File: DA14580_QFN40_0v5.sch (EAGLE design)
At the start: 29 parts, among them CON1 CON_TC2030-CTL-NL, IC1 1265-1137-1-ND, IC2 74LVC1G00DBV, IC3 IC_LDO_XX1117_5, U1 DA14583-AT2, X1 SSW-114-02-S-S, X2 SSW-114-02-S-S

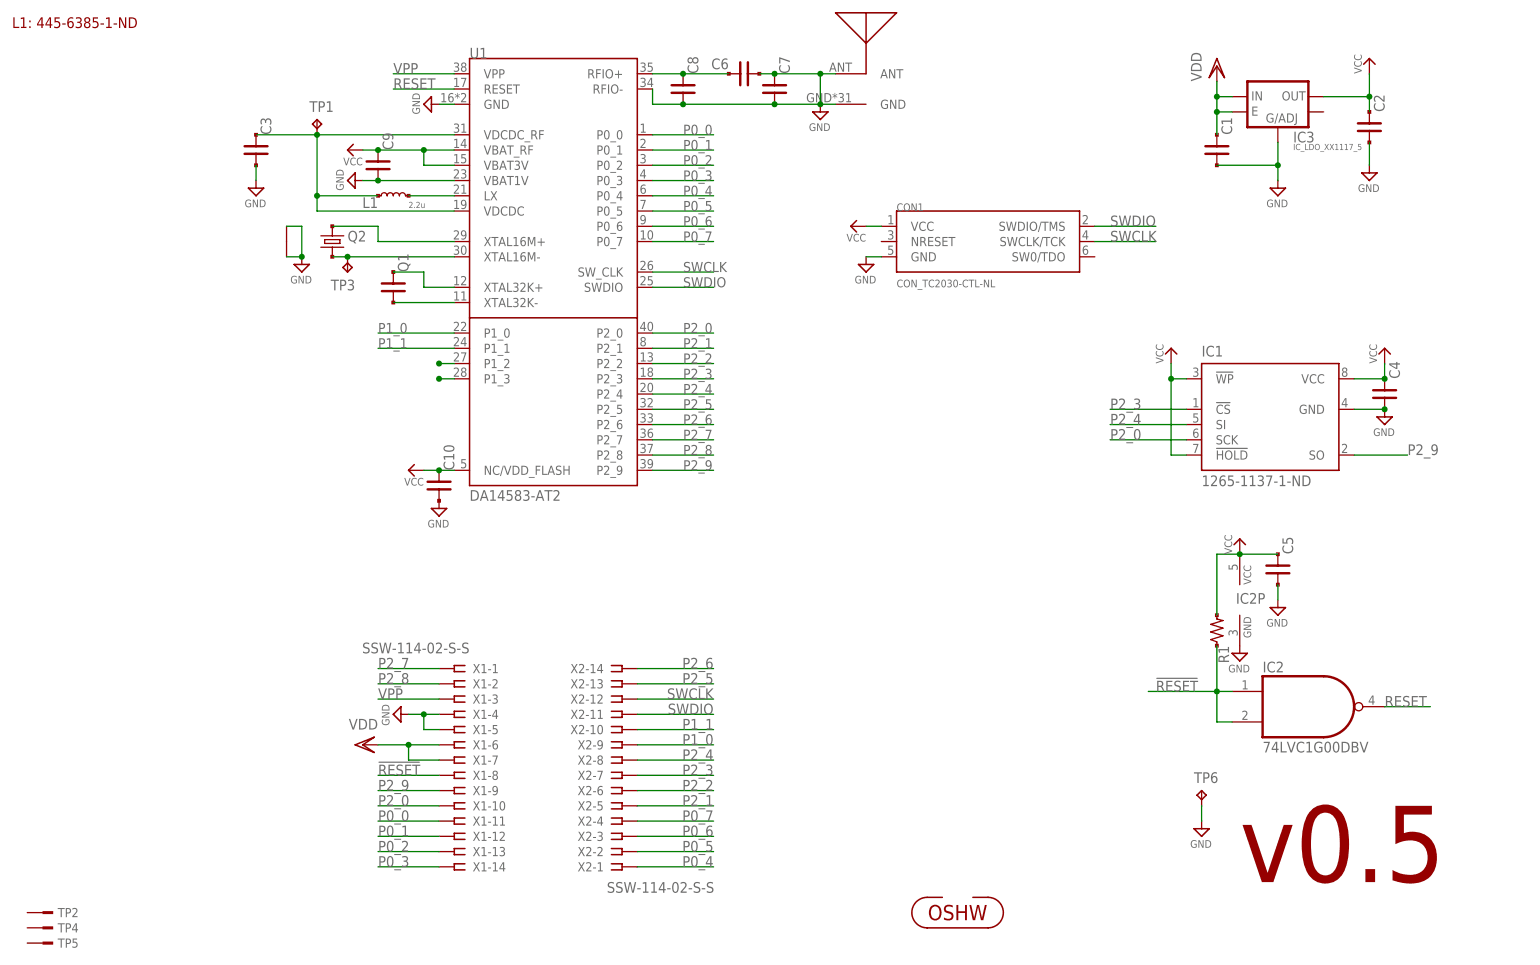
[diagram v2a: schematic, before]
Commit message: [ 58x ] add fiducial; increase sub board width; move whole board by 1mm North-East; add some value to parts
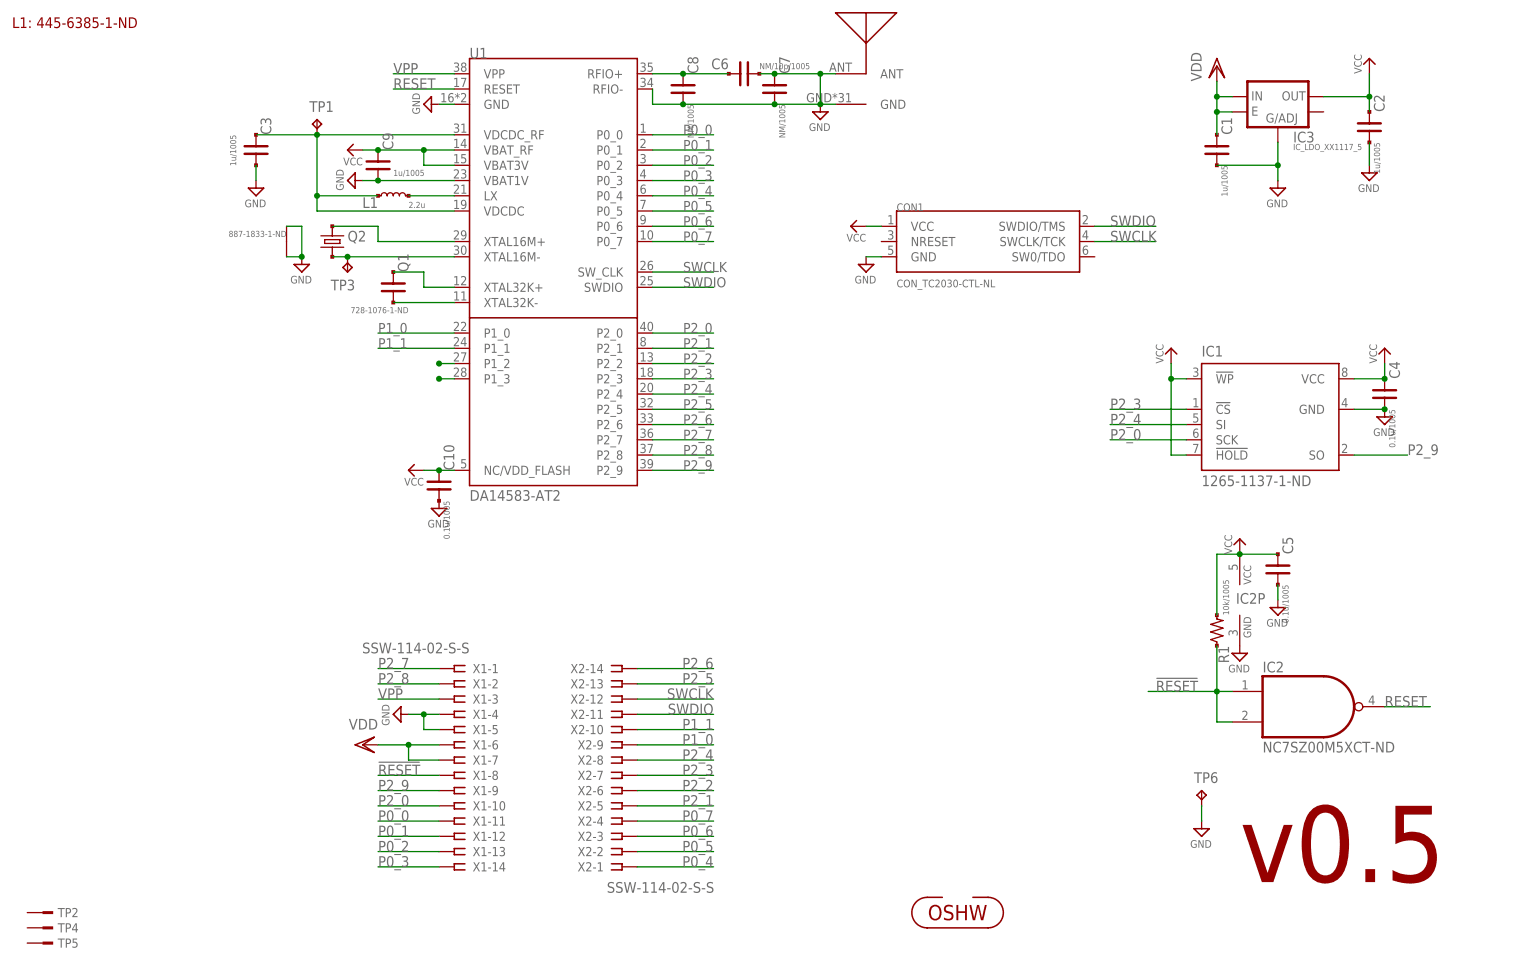
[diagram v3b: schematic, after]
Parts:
- C1, C2, C3, C9: value (none) -> 1u/1005
- C10, C4, C5: value (none) -> 0.1u/1005
- C6: value (none) -> NM/10p/1005
- C7, C8: value (none) -> NM/1005
- IC2: value 74LVC1G00DBV -> NC7SZ00M5XCT-ND
- Q1: value (none) -> 728-1076-1-ND
- Q2: value (none) -> 887-1833-1-ND
- R1: value (none) -> 10k/1005
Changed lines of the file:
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@@
 <part name="VDD1" library="supply1" deviceset="VDD" device=""/>
 <part name="P+1" library="mylib" deviceset="VCC" device=""/>
-<part name="Q1" library="mylib" deviceset="C_PAD_PAD_" device="3216"/>
+<part name="Q1" library="mylib" deviceset="C_PAD_PAD_" device="3216" value="728-1076-1-ND"/>
 <part name="SUPPLY7" library="mylib" deviceset="GND" device=""/>
 <part name="SUPPLY8" library="mylib" deviceset="GND" device=""/>
 <part name="P+2" library="mylib" deviceset="VCC" device=""/>
-<part name="C1" library="mylib" deviceset="C_PAD_PAD_" device="1005"/>
-<part name="C2" library="mylib" deviceset="C_PAD_PAD_" device="1005"/>
+<part name="C1" library="mylib" deviceset="C_PAD_PAD_" device="1005" value="1u/1005"/>
+<part name="C2" library="mylib" deviceset="C_PAD_PAD_" device="1005" value="1u/1005"/>
 <part name="SUPPLY9" library="mylib" deviceset="GND" device=""/>
 <part name="SUPPLY11" library="mylib" deviceset="GND" device=""/>
-<part name="C3" library="mylib" deviceset="C_PAD_PAD_" device="1005"/>
+<part name="C3" library="mylib" deviceset="C_PAD_PAD_" device="1005" value="1u/1005"/>
 <part name="L1" library="mylib" deviceset="INDUCTOR" device="_1608" value="2.2u"/>
-<part name="R1" library="mylib" deviceset="R_US_PAD_PAD" device="_1005"/>
+<part name="R1" library="mylib" deviceset="R_US_PAD_PAD" device="_1005" value="10k/1005"/>
 <part name="IC1" library="mylib" deviceset="IC_MEMORY_8P_*" device="_SOP" technology="AT25XE011" value="1265-1137-1-ND"/>
 <part name="P+3" library="mylib" deviceset="VCC" device=""/>
-<part name="C4" library="mylib" deviceset="C_PAD_PAD_" device="1005"/>
+<part name="C4" library="mylib" deviceset="C_PAD_PAD_" device="1005" value="0.1u/1005"/>
 <part name="SUPPLY13" library="mylib" deviceset="GND" device=""/>
 <part name="TP1" library="testpad_local" deviceset="TP" device="TP07R" value="TPTP07R"/>
@@
 <part name="X2" library="con-samtec.local" deviceset="SSW-114-02-S-S" device=""/>
 <part name="SUPPLY10" library="mylib" deviceset="GND" device=""/>
-<part name="C5" library="mylib" deviceset="C_PAD_PAD_" device="1005"/>
+<part name="C5" library="mylib" deviceset="C_PAD_PAD_" device="1005" value="0.1u/1005"/>
 <part name="SUPPLY12" library="mylib" deviceset="GND" device=""/>
 <part name="P+4" library="mylib" deviceset="VCC" device=""/>
@@
 <part name="P+5" library="mylib" deviceset="VCC" device=""/>
 <part name="IC3" library="mylib" deviceset="IC_LDO_XX1117_5" device=""/>
-<part name="IC2" library="74xx-little-us_local" deviceset="74*1G00" device="DBV" technology="LVC"/>
+<part name="IC2" library="74xx-little-us_local" deviceset="74*1G00" device="DBV" technology="LVC" value="NC7SZ00M5XCT-ND"/>
 <part name="TP6" library="testpad_local" deviceset="TP" device="PAD1-13"/>
-<part name="C6" library="mylib" deviceset="C_PAD_PAD_" device="1005"/>
-<part name="C7" library="mylib" deviceset="C_PAD_PAD_" device="1005"/>
-<part name="C8" library="mylib" deviceset="C_PAD_PAD_" device="1005"/>
-<part name="C9" library="mylib" deviceset="C_PAD_PAD_" device="1005"/>
-<part name="C10" library="mylib" deviceset="C_PAD_PAD_" device="1005"/>
+<part name="C6" library="mylib" deviceset="C_PAD_PAD_" device="1005" value="NM/10p/1005"/>
+<part name="C7" library="mylib" deviceset="C_PAD_PAD_" device="1005" value="NM/1005"/>
+<part name="C8" library="mylib" deviceset="C_PAD_PAD_" device="1005" value="NM/1005"/>
+<part name="C9" library="mylib" deviceset="C_PAD_PAD_" device="1005" value="1u/1005"/>
+<part name="C10" library="mylib" deviceset="C_PAD_PAD_" device="1005" value="0.1u/1005"/>
 <part name="SUPPLY15" library="mylib" deviceset="GND" device=""/>
 <part name="SUPPLY16" library="mylib" deviceset="GND" device=""/>
@@
 <part name="U$2" library="mylib" deviceset="ICON_OSHW" device=""/>
 <part name="P+6" library="mylib" deviceset="VCC" device=""/>
-<part name="Q2" library="mylib" deviceset="CLOCK_CRYSTAL_4" device="_2520"/>
+<part name="Q2" library="mylib" deviceset="CLOCK_CRYSTAL_4" device="_2520" value="887-1833-1-ND"/>
 <part name="P+7" library="mylib" deviceset="VCC" device=""/>
 <part name="TP2" library="mylib" deviceset="TESTPAD" device="_F"/>
@@
 <instance part="VDD1" gate="G$1" x="213.36" y="161.29"/>
 <instance part="P+1" gate="VCC" x="238.76" y="162.56"/>
-<instance part="Q1" gate="G$1" x="76.2" y="124.46"/>
+<instance part="Q1" gate="G$1" x="76.2" y="124.46" smashed="yes">
+<attribute name="NAME" x="78.74" y="127" size="1.778" layer="95" rot="R90"/>
+<attribute name="VALUE" x="78.74" y="121.158" size="1.016" layer="96" rot="R180"/>
+</instance>
 <instance part="SUPPLY7" gate="GND" x="60.96" y="127"/>
 <instance part="SUPPLY8" gate="GND" x="223.52" y="139.7"/>
@@
 <instance part="SUPPLY9" gate="GND" x="238.76" y="142.24"/>
 <instance part="SUPPLY11" gate="GND" x="53.34" y="139.7"/>
-<instance part="C3" gate="G$1" x="53.34" y="147.32"/>
+<instance part="C3" gate="G$1" x="53.34" y="147.32" smashed="yes">
+<attribute name="NAME" x="55.88" y="149.86" size="1.778" layer="95" rot="R90"/>
+<attribute name="VALUE" x="49.022" y="149.86" size="1.016" layer="96" rot="R270"/>
+</instance>
 <instance part="L1" gate="G$1" x="76.2" y="139.7"/>
 <instance part="R1" gate="G$1" x="213.36" y="67.31" rot="R90"/>
@@
 <instance part="C7" gate="G$1" x="139.7" y="157.48"/>
 <instance part="C8" gate="G$1" x="124.46" y="157.48"/>
-<instance part="C9" gate="G$1" x="73.66" y="144.78"/>
+<instance part="C9" gate="G$1" x="73.66" y="144.78" smashed="yes">
+<attribute name="NAME" x="76.2" y="147.32" size="1.778" layer="95" rot="R90"/>
+<attribute name="VALUE" x="76.2" y="143.002" size="1.016" layer="96"/>
+</instance>
 <instance part="C10" gate="G$1" x="83.82" y="91.44"/>
 <instance part="SUPPLY15" gate="GND" x="83.82" y="86.36"/>
@@
 <instance part="Q2" gate="G$1" x="66.04" y="132.08" smashed="yes" rot="R270">
 <attribute name="NAME" x="68.58" y="132.08" size="1.778" layer="95"/>
-<attribute name="VALUE" x="66.802" y="129.54" size="1.016" layer="96" rot="R270"/>
+<attribute name="VALUE" x="58.42" y="133.858" size="1.016" layer="96" rot="R180"/>
 </instance>
 <instance part="P+7" gate="VCC" x="241.3" y="114.3"/>

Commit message: [ 58x ] library update
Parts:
- C1, C2, C3, C9: value 1u/1005 -> (none); device mylib:C_PAD_PAD_1005 -> mylib:C_SMD_1.0U_1005
- C10, C4, C5: value 0.1u/1005 -> (none); device mylib:C_PAD_PAD_1005 -> mylib:C_SMD_0.1U_1005
- C6: value NM/10p/1005 -> NM; device mylib:C_PAD_PAD_1005 -> mylib:C_SMD_10P_1005
- C7, C8: value NM/1005 -> (none); device mylib:C_PAD_PAD_1005 -> mylib:C_SMD__1005
- L1: value 2.2u -> INDUCTOR_2.2U_1608; device mylib:INDUCTOR_1608 -> mylib:INDUCTOR_2.2U_1608
- Q1: device mylib:C_PAD_PAD_3216 -> mylib:CLOCK_CRYSTAL_FC-135
- R1: value 10k/1005 -> (none); device mylib:R_US_PAD_PAD_1005 -> mylib:R_US_10K_1005
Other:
- moved on the sheet: L1
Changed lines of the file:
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@@
 <part name="VDD1" library="supply1" deviceset="VDD" device=""/>
 <part name="P+1" library="mylib" deviceset="VCC" device=""/>
-<part name="Q1" library="mylib" deviceset="C_PAD_PAD_" device="3216" value="728-1076-1-ND"/>
+<part name="Q1" library="mylib" deviceset="CLOCK_CRYSTAL" device="_FC-135" value="728-1076-1-ND"/>
 <part name="SUPPLY7" library="mylib" deviceset="GND" device=""/>
 <part name="SUPPLY8" library="mylib" deviceset="GND" device=""/>
 <part name="P+2" library="mylib" deviceset="VCC" device=""/>
-<part name="C1" library="mylib" deviceset="C_PAD_PAD_" device="1005" value="1u/1005"/>
-<part name="C2" library="mylib" deviceset="C_PAD_PAD_" device="1005" value="1u/1005"/>
+<part name="C1" library="mylib" deviceset="C_SMD_*" device="_1005" technology="1.0U"/>
+<part name="C2" library="mylib" deviceset="C_SMD_*" device="_1005" technology="1.0U"/>
 <part name="SUPPLY9" library="mylib" deviceset="GND" device=""/>
 <part name="SUPPLY11" library="mylib" deviceset="GND" device=""/>
-<part name="C3" library="mylib" deviceset="C_PAD_PAD_" device="1005" value="1u/1005"/>
-<part name="L1" library="mylib" deviceset="INDUCTOR" device="_1608" value="2.2u"/>
-<part name="R1" library="mylib" deviceset="R_US_PAD_PAD" device="_1005" value="10k/1005"/>
+<part name="C3" library="mylib" deviceset="C_SMD_*" device="_1005" technology="1.0U"/>
+<part name="L1" library="mylib" deviceset="INDUCTOR_" device="_1608" technology="2.2U" value=""/>
+<part name="R1" library="mylib" deviceset="R_US_*" device="_1005" technology="10K"/>
 <part name="IC1" library="mylib" deviceset="IC_MEMORY_8P_*" device="_SOP" technology="AT25XE011" value="1265-1137-1-ND"/>
 <part name="P+3" library="mylib" deviceset="VCC" device=""/>
-<part name="C4" library="mylib" deviceset="C_PAD_PAD_" device="1005" value="0.1u/1005"/>
+<part name="C4" library="mylib" deviceset="C_SMD_*" device="_1005" technology="0.1U"/>
 <part name="SUPPLY13" library="mylib" deviceset="GND" device=""/>
 <part name="TP1" library="testpad_local" deviceset="TP" device="TP07R" value="TPTP07R"/>
@@
 <part name="X2" library="con-samtec.local" deviceset="SSW-114-02-S-S" device=""/>
 <part name="SUPPLY10" library="mylib" deviceset="GND" device=""/>
-<part name="C5" library="mylib" deviceset="C_PAD_PAD_" device="1005" value="0.1u/1005"/>
+<part name="C5" library="mylib" deviceset="C_SMD_*" device="_1005" technology="0.1U"/>
 <part name="SUPPLY12" library="mylib" deviceset="GND" device=""/>
 <part name="P+4" library="mylib" deviceset="VCC" device=""/>
@@
 <part name="IC2" library="74xx-little-us_local" deviceset="74*1G00" device="DBV" technology="LVC" value="NC7SZ00M5XCT-ND"/>
 <part name="TP6" library="testpad_local" deviceset="TP" device="PAD1-13"/>
-<part name="C6" library="mylib" deviceset="C_PAD_PAD_" device="1005" value="NM/10p/1005"/>
-<part name="C7" library="mylib" deviceset="C_PAD_PAD_" device="1005" value="NM/1005"/>
-<part name="C8" library="mylib" deviceset="C_PAD_PAD_" device="1005" value="NM/1005"/>
-<part name="C9" library="mylib" deviceset="C_PAD_PAD_" device="1005" value="1u/1005"/>
-<part name="C10" library="mylib" deviceset="C_PAD_PAD_" device="1005" value="0.1u/1005"/>
+<part name="C6" library="mylib" deviceset="C_SMD_*" device="_1005" technology="10P" value="NM"/>
+<part name="C7" library="mylib" deviceset="C_SMD_*" device="_1005"/>
+<part name="C8" library="mylib" deviceset="C_SMD_*" device="_1005"/>
+<part name="C9" library="mylib" deviceset="C_SMD_*" device="_1005" technology="1.0U"/>
+<part name="C10" library="mylib" deviceset="C_SMD_*" device="_1005" technology="0.1U"/>
 <part name="SUPPLY15" library="mylib" deviceset="GND" device=""/>
 <part name="SUPPLY16" library="mylib" deviceset="GND" device=""/>
@@
 <attribute name="VALUE" x="49.022" y="149.86" size="1.016" layer="96" rot="R270"/>
 </instance>
-<instance part="L1" gate="G$1" x="76.2" y="139.7"/>
+<instance part="L1" gate="G$1" x="73.66" y="139.7" smashed="yes">
+<attribute name="NAME" x="71.12" y="139.446" size="1.778" layer="95" rot="R180"/>
+<attribute name="VALUE" x="71.12" y="137.668" size="1.016" layer="96"/>
+</instance>
 <instance part="R1" gate="G$1" x="213.36" y="67.31" rot="R90"/>
 <instance part="IC1" gate="G$1" x="223.52" y="101.6"/>
@@
 <instance part="C4" gate="G$1" x="241.3" y="106.68"/>
 <instance part="SUPPLY13" gate="GND" x="241.3" y="101.6"/>
-<instance part="TP1" gate="G$1" x="63.5" y="152.4"/>
+<instance part="TP1" gate="G$1" x="63.5" y="152.4" smashed="yes">
+<attribute name="NAME" x="62.23" y="153.67" size="1.778" layer="95"/>
+</instance>
 <instance part="X1" gate="-1" x="86.36" y="60.96" rot="MR0"/>
 <instance part="X1" gate="-2" x="86.36" y="58.42" rot="MR0"/>
@@
 <instance part="SUPPLY12" gate="GND" x="223.52" y="69.85"/>
 <instance part="P+4" gate="VCC" x="217.17" y="82.55"/>
-<instance part="TP3" gate="G$1" x="68.58" y="127" rot="R180"/>
+<instance part="TP3" gate="G$1" x="68.58" y="127" smashed="yes" rot="R180">
+<attribute name="NAME" x="69.85" y="125.73" size="1.778" layer="95" rot="R180"/>
+</instance>
 <instance part="P+5" gate="VCC" x="78.74" y="93.98" rot="R90"/>
 <instance part="IC3" gate="G$1" x="223.52" y="158.75"/>
@@
 <pinref part="U1" gate="G$1" pin="LX"/>
 <pinref part="L1" gate="G$1" pin="2"/>
-<wire x1="86.36" y1="139.7" x2="78.74" y2="139.7" width="0.1524" layer="91"/>
+<wire x1="86.36" y1="139.7" x2="76.2" y2="139.7" width="0.1524" layer="91"/>
 </segment>
 </net>
@@
 <wire x1="63.5" y1="149.86" x2="63.5" y2="139.7" width="0.1524" layer="91"/>
 <pinref part="U1" gate="G$1" pin="VDCDC"/>
-<wire x1="73.66" y1="139.7" x2="63.5" y2="139.7" width="0.1524" layer="91"/>
+<wire x1="71.12" y1="139.7" x2="63.5" y2="139.7" width="0.1524" layer="91"/>
 <wire x1="63.5" y1="139.7" x2="63.5" y2="137.16" width="0.1524" layer="91"/>
 <wire x1="63.5" y1="137.16" x2="86.36" y2="137.16" width="0.1524" layer="91"/>
